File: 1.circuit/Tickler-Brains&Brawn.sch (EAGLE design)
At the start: 30 parts, among them IC1 MCP23017, J1 PN61729-S, U1 PIC18F4550_40, X1 20Mhz

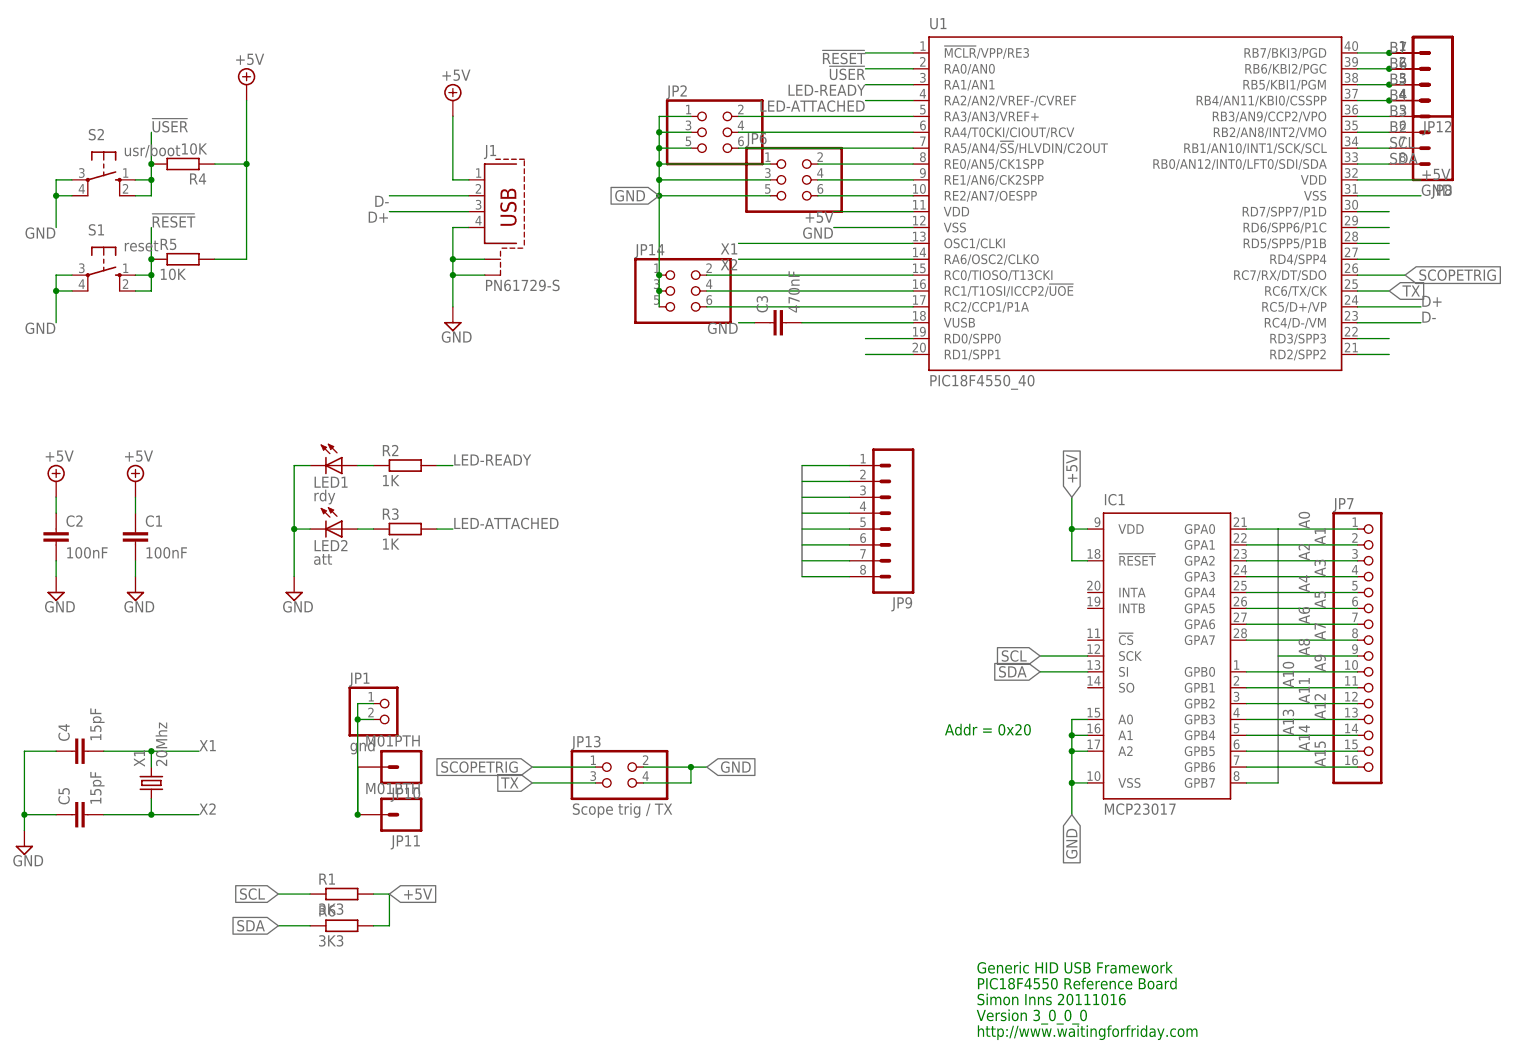
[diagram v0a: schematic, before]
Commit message: slight change to board - rx reinstated as its hard to use the usart module with a bifurcated tx and rx pair
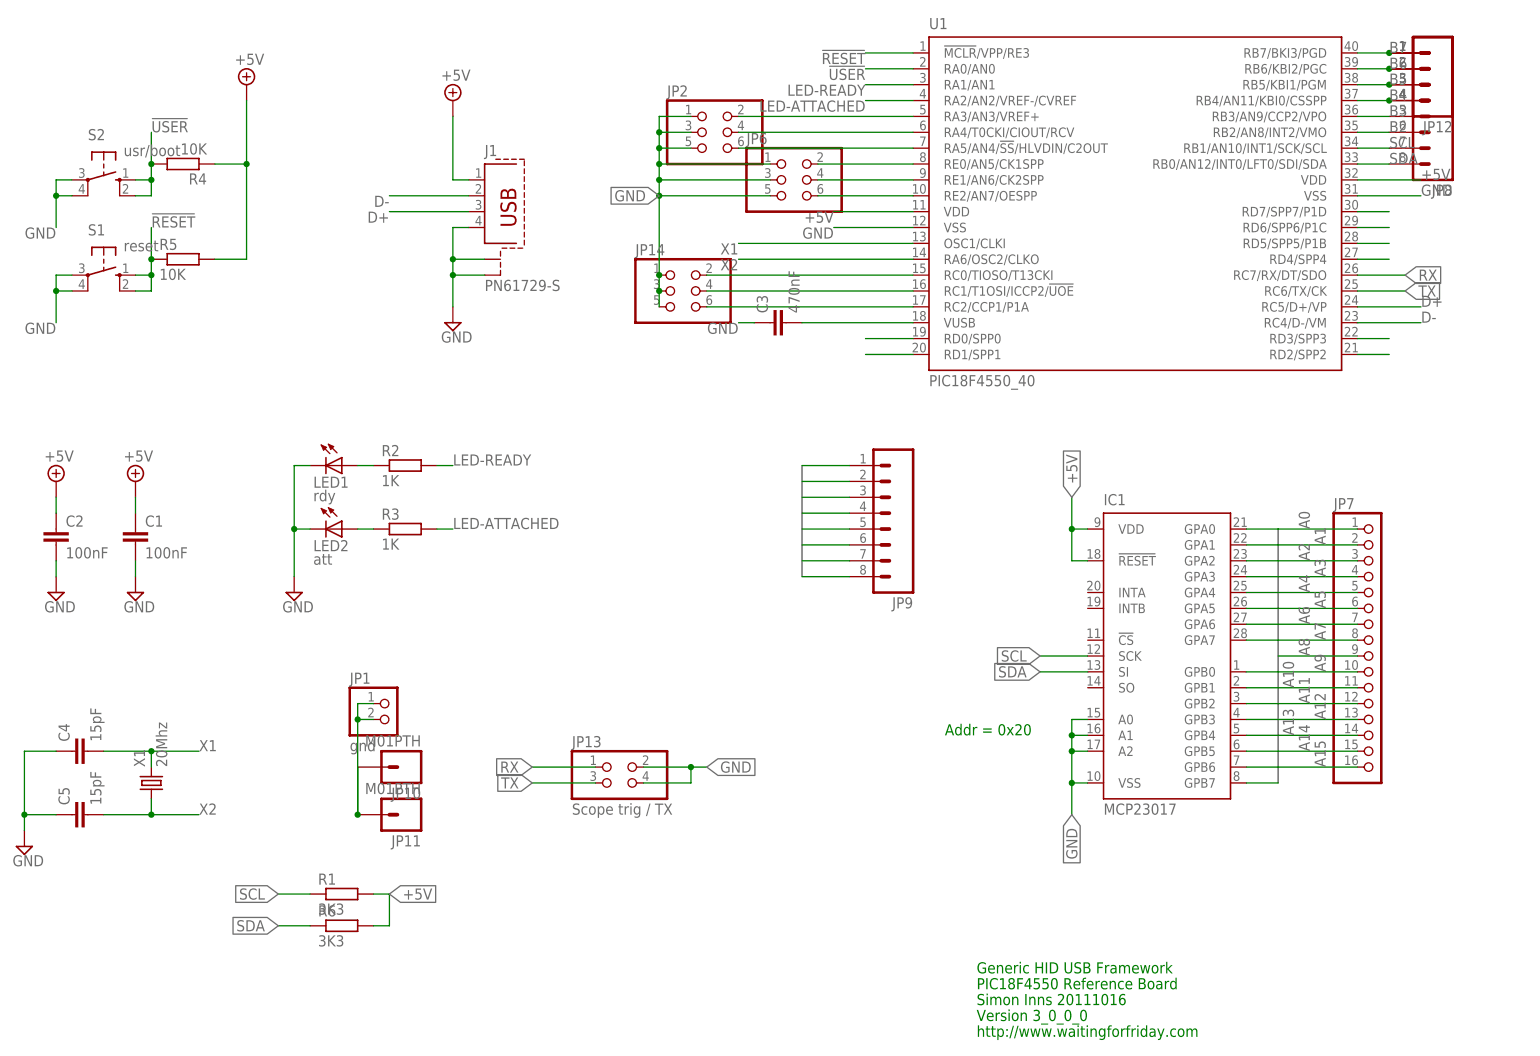
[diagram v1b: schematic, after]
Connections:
- net SCOPETRIG renamed RX
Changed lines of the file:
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@@
-</segment>
-</net>
-<net name="SCOPETRIG" class="0">
-<segment>
-<pinref part="U1" gate="G$1" pin="RC7/RX/DT/SDO"/>
-<wire x1="226.06" y1="129.54" x2="233.68" y2="129.54" width="0.1524" layer="91"/>
-<label x="233.68" y="129.54" size="1.778" layer="95" xref="yes"/>
-</segment>
-<segment>
-<pinref part="JP13" gate="A" pin="1"/>
-<wire x1="104.14" y1="50.8" x2="93.98" y2="50.8" width="0.1524" layer="91"/>
-<label x="93.98" y="50.8" size="1.778" layer="95" rot="R180" xref="yes"/>
 </segment>
 </net>
@@
 <segment>
 <pinref part="U1" gate="G$1" pin="RC6/TX/CK"/>
-<wire x1="231.14" y1="127" x2="226.06" y2="127" width="0.1524" layer="91"/>
-<label x="231.14" y="127" size="1.778" layer="95" xref="yes"/>
+<wire x1="233.68" y1="127" x2="226.06" y2="127" width="0.1524" layer="91"/>
+<label x="233.68" y="127" size="1.778" layer="95" xref="yes"/>
 </segment>
 <segment>
@@
 </segment>
 </net>
+<net name="RX" class="0">
+<segment>
+<pinref part="U1" gate="G$1" pin="RC7/RX/DT/SDO"/>
+<wire x1="226.06" y1="129.54" x2="233.68" y2="129.54" width="0.1524" layer="91"/>
+<label x="233.68" y="129.54" size="1.778" layer="95" xref="yes"/>
+</segment>
+<segment>
+<pinref part="JP13" gate="A" pin="1"/>
+<wire x1="104.14" y1="50.8" x2="93.98" y2="50.8" width="0.1524" layer="91"/>
+<label x="93.98" y="50.8" size="1.778" layer="95" rot="R180" xref="yes"/>
+</segment>
+</net>
